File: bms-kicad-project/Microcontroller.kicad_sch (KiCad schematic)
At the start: 40 parts, among them J1 12402012E212A, J2 DEBUG, J3 Conn_02x18_Odd_Even, J4 Conn_02x18_Odd_Even, Q13 BSS308PE_H6327, SW1 KMR223G LFG, SW2 KMR223G LFG, U2 W25Q128JVSIQ TR, U3 NCP1117ST33T3G, U4 RP2040, X1 ABM8-272-T3

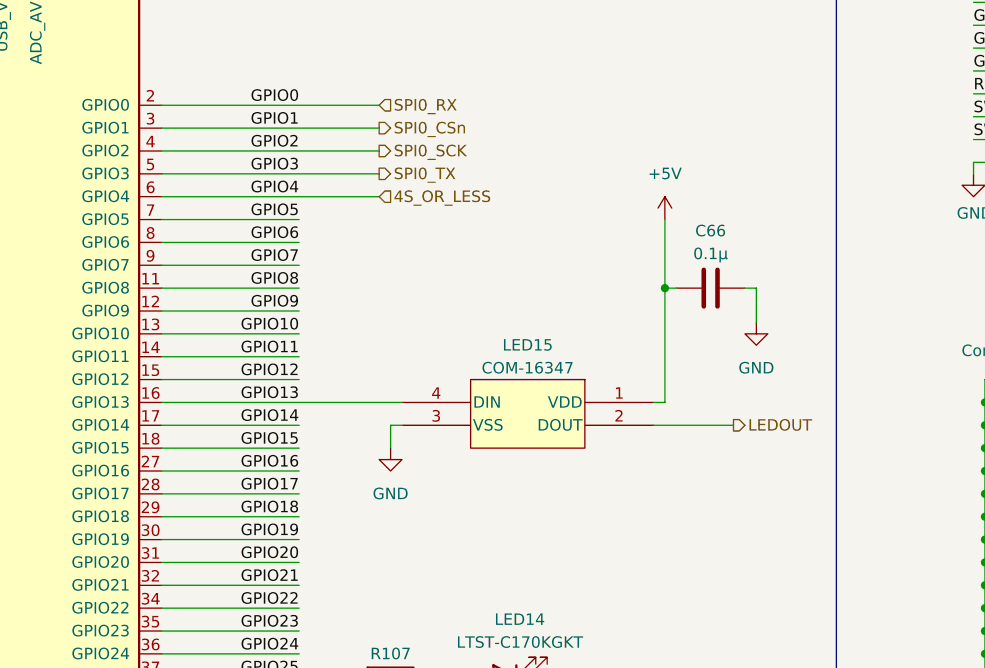
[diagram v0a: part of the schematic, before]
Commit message: Wired up most external connections
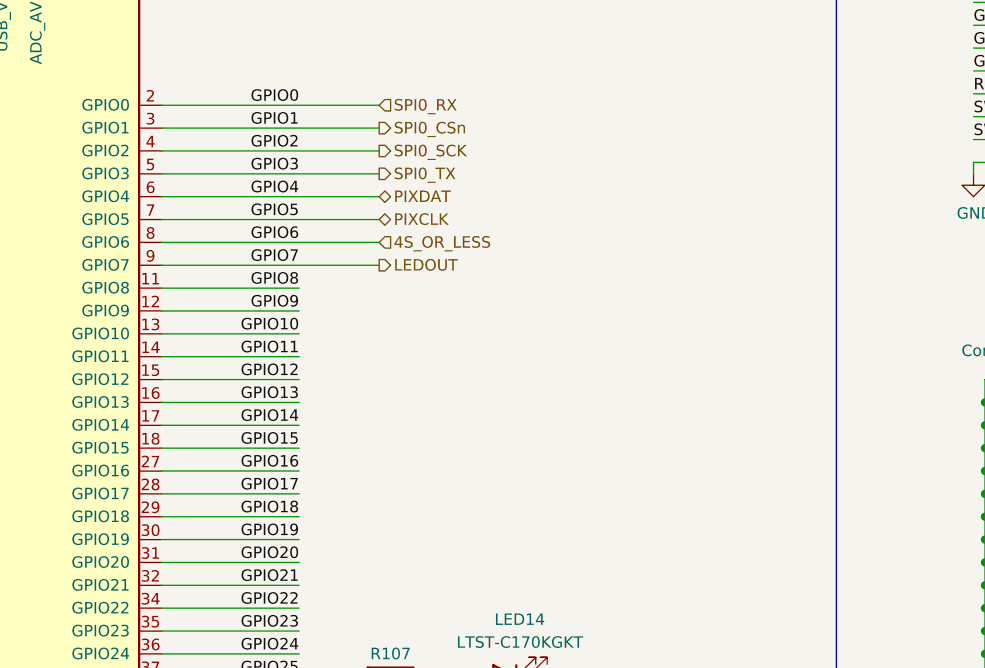
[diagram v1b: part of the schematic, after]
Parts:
- removed C66: 0.1µ, FixedWing:G-21_MUR, symbol FixedWing:GCM21BR72A104KA37L
- removed LED15: COM-16347, FixedWing:COM-16347_SPK, symbol FixedWing:COM-16347
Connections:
- net GPIO6 is gone; now on net 4S_OR_LESS: J3.16 (Pin_16), U4.8 (GPIO6)
- net GPIO7 is gone; now on net LEDOUT: J3.18 (Pin_18), U4.9 (GPIO7)
- net 4S_OR_LESS: no longer J3.12 (Pin_12), U4.6 (GPIO4)
- net GPIO5 renamed PIXCLK
- new net PIXDAT: J3.12 (Pin_12), U4.6 (GPIO4)
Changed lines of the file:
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@@
   (junction (at 26.67 146.05) (diameter 0) (color 0 0 0 0)
   )
-  (junction (at 344.17 123.19) (diameter 0) (color 0 0 0 0)
-  )
   (junction (at 405.13 81.28) (diameter 0) (color 0 0 0 0)
   )
@@
     (stroke (width 0) (type default))
   )
-  (wire (pts (xy 344.17 123.19) (xy 344.17 135.89))
-    (stroke (width 0) (type default))
-  )
   (wire (pts (xy 405.13 76.2) (xy 405.13 78.74))
     (stroke (width 0) (type default))
@@
     (stroke (width 0) (type default))
   )
-  (wire (pts (xy 342.9 138.43) (xy 351.79 138.43))
-    (stroke (width 0) (type default))
-  )
   (wire (pts (xy 288.29 166.37) (xy 309.88 166.37))
     (stroke (width 0) (type default))
   )
-  (wire (pts (xy 344.17 123.19) (xy 344.17 115.57))
-    (stroke (width 0) (type default))
-  )
   (wire (pts (xy 247.65 72.39) (xy 254 72.39))
     (stroke (width 0) (type default))
@@
     (stroke (width 0) (type default))
   )
+  (wire (pts (xy 288.29 120.65) (xy 312.42 120.65))
+    (stroke (width 0) (type default))
+  )
   (wire (pts (xy 55.88 128.27) (xy 55.88 121.92))
     (stroke (width 0) (type default))
@@
     (stroke (width 0) (type default))
   )
-  (wire (pts (xy 342.9 135.89) (xy 344.17 135.89))
-    (stroke (width 0) (type default))
-  )
   (wire (pts (xy 259.08 85.09) (xy 259.08 72.39))
     (stroke (width 0) (type default))
@@
     (stroke (width 0) (type default))
   )
+  (wire (pts (xy 288.29 135.89) (xy 303.53 135.89))
+    (stroke (width 0) (type default))
+  )
   (wire (pts (xy 147.32 137.16) (xy 147.32 165.1))
     (stroke (width 0) (type default))
@@
     (stroke (width 0) (type default))
   )
-  (wire (pts (xy 344.17 123.19) (xy 345.44 123.19))
-    (stroke (width 0) (type default))
-  )
   (wire (pts (xy 55.88 130.81) (xy 55.88 139.7))
     (stroke (width 0) (type default))
@@
     (stroke (width 0) (type default))
   )
-  (wire (pts (xy 313.69 138.43) (xy 313.69 140.97))
-    (stroke (width 0) (type default))
-  )
   (wire (pts (xy 379.73 163.83) (xy 379.73 166.37))
     (stroke (width 0) (type default))
@@
     (stroke (width 0) (type default))
   )
-  (wire (pts (xy 288.29 118.11) (xy 303.53 118.11))
+  (wire (pts (xy 288.29 118.11) (xy 312.42 118.11))
     (stroke (width 0) (type default))
   )
@@
     (stroke (width 0) (type default))
   )
-  (wire (pts (xy 288.29 120.65) (xy 303.53 120.65))
-    (stroke (width 0) (type default))
-  )
   (wire (pts (xy 227.33 68.58) (xy 227.33 67.31))
     (stroke (width 0) (type default))
@@
     (stroke (width 0) (type default))
   )
-  (wire (pts (xy 354.33 123.19) (xy 353.06 123.19))
-    (stroke (width 0) (type default))
-  )
   (wire (pts (xy 391.16 93.98) (xy 378.46 93.98))
     (stroke (width 0) (type default))
@@
     (stroke (width 0) (type default))
   )
-  (wire (pts (xy 288.29 135.89) (xy 314.96 135.89))
-    (stroke (width 0) (type default))
-  )
   (wire (pts (xy 339.09 54.61) (xy 327.66 54.61))
     (stroke (width 0) (type default))
@@
     (stroke (width 0) (type default))
   )
-  (wire (pts (xy 288.29 115.57) (xy 303.53 115.57))
+  (wire (pts (xy 288.29 115.57) (xy 312.42 115.57))
     (stroke (width 0) (type default))
   )
@@
     (stroke (width 0) (type default))
   )
-  (wire (pts (xy 314.96 138.43) (xy 313.69 138.43))
-    (stroke (width 0) (type default))
-  )
   (wire (pts (xy 36.83 160.02) (xy 142.24 160.02))
     (stroke (width 0) (type default))
@@
     (stroke (width 0) (type default))
   )
-  (wire (pts (xy 354.33 123.19) (xy 354.33 127))
-    (stroke (width 0) (type default))
-  )
   (wire (pts (xy 316.23 52.07) (xy 316.23 54.61))
     (stroke (width 0) (type default))
@@
     (effects (font (size 1.27 1.27)) (justify left))
   )
-  (hierarchical_label "SPI0_SCK" (shape output) (at 312.42 107.95 0) (fields_autoplaced)
+  (hierarchical_label "LEDOUT" (shape output) (at 312.42 120.65 0) (fields_autoplaced)
     (effects (font (size 1.27 1.27)) (justify left))
   )
-  (hierarchical_label "LEDOUT" (shape output) (at 351.79 138.43 0) (fields_autoplaced)
+  (hierarchical_label "SPI0_SCK" (shape output) (at 312.42 107.95 0) (fields_autoplaced)
     (effects (font (size 1.27 1.27)) (justify left))
   )
-  (hierarchical_label "4S_OR_LESS" (shape input) (at 312.42 113.03 0) (fields_autoplaced)
+  (hierarchical_label "4S_OR_LESS" (shape input) (at 312.42 118.11 0) (fields_autoplaced)
     (effects (font (size 1.27 1.27)) (justify left))
   )
@@
     (effects (font (size 1.27 1.27)) (justify left))
   )
+  (hierarchical_label "PIXDAT" (shape bidirectional) (at 312.42 113.03 0) (fields_autoplaced)
+    (effects (font (size 1.27 1.27)) (justify left))
+  )
+  (hierarchical_label "PIXCLK" (shape bidirectional) (at 312.42 115.57 0) (fields_autoplaced)
+    (effects (font (size 1.27 1.27)) (justify left))
+  )
   (hierarchical_label "SPI0_RX" (shape input) (at 312.42 102.87 0) (fields_autoplaced)
     (effects (font (size 1.27 1.27)) (justify left))
@@
     )
   )
-  (symbol (lib_id "power:+5V") (at 344.17 115.57 0) (unit 1)
-    (in_bom yes) (on_board yes) (dnp no) (fields_autoplaced)
-    (property "Reference" "#PWR062" (at 344.17 119.38 0)
-      (effects (font (size 1.27 1.27)) hide)
-    )
-    (property "Value" "+5V" (at 344.17 110.49 0)
-      (effects (font (size 1.27 1.27)))
-    )
-    (property "Footprint" "" (at 344.17 115.57 0)
-      (effects (font (size 1.27 1.27)) hide)
-    )
-    (property "Datasheet" "" (at 344.17 115.57 0)
-      (effects (font (size 1.27 1.27)) hide)
-    )
-    (pin "1")
-    (instances
-      (project "bms-board"
-        (path "/8a7831d1-a913-4f04-8780-225d2234b41d/449bb263-23d7-4f07-b4f7-6cd2e161d267"
-          (reference "#PWR062") (unit 1)
-        )
-      )
-    )
-  )
-  (symbol (lib_id "FixedWing:COM-16347") (at 342.9 135.89 0) (mirror y) (unit 1)
-    (in_bom yes) (on_board yes) (dnp no)
-    (property "Reference" "LED15" (at 328.93 129.54 0)
-      (effects (font (size 1.27 1.27)))
-    )
-    (property "Value" "COM-16347" (at 328.93 132.08 0)
-      (effects (font (size 1.27 1.27)))
-    )
-    (property "Footprint" "FixedWing:COM-16347_SPK" (at 342.9 123.19 0)
-      (effects (font (size 1.27 1.27) italic) hide)
-    )
-    (property "Datasheet" "https://cdn.sparkfun.com/datasheets/BreakoutBoards/WS2812B.pdf" (at 342.9 123.19 0)
-      (effects (font (size 1.27 1.27) italic) hide)
-    )
-    (property "Manufacturer" "SparkFun Electronics" (at 342.9 123.19 0)
-      (effects (font (size 1.27 1.27)) hide)
-    )
-    (property "Manufacturer Part Number" "COM-16347" (at 342.9 123.19 0)
-      (effects (font (size 1.27 1.27)) hide)
-    )
-    (pin "4")
-    (pin "3")
-    (pin "2")
-    (pin "1")
-    (instances
-      (project "bms-board"
-        (path "/8a7831d1-a913-4f04-8780-225d2234b41d/449bb263-23d7-4f07-b4f7-6cd2e161d267"
-          (reference "LED15") (unit 1)
-        )
-      )
-    )
-  )
   (symbol (lib_id "power:GND") (at 336.55 170.18 0) (unit 1)
     (in_bom yes) (on_board yes) (dnp no) (fields_autoplaced)
@@
     )
   )
-  (symbol (lib_id "power:GND") (at 313.69 140.97 0) (unit 1)
-    (in_bom yes) (on_board yes) (dnp no) (fields_autoplaced)
-    (property "Reference" "#PWR063" (at 313.69 147.32 0)
-      (effects (font (size 1.27 1.27)) hide)
-    )
-    (property "Value" "GND" (at 313.69 146.05 0)
-      (effects (font (size 1.27 1.27)))
-    )
-    (property "Footprint" "" (at 313.69 140.97 0)
-      (effects (font (size 1.27 1.27)) hide)
-    )
-    (property "Datasheet" "" (at 313.69 140.97 0)
-      (effects (font (size 1.27 1.27)) hide)
-    )
-    (pin "1")
-    (instances
-      (project "bms-board"
-        (path "/8a7831d1-a913-4f04-8780-225d2234b41d/449bb263-23d7-4f07-b4f7-6cd2e161d267"
-          (reference "#PWR063") (unit 1)
-        )
-      )
-    )
-  )
   (symbol (lib_id "FixedWing:KMR223G_LFG") (at 57.15 128.27 0) (unit 1)
     (in_bom yes) (on_board yes) (dnp no)
@@
     )
   )
-  (symbol (lib_id "power:GND") (at 354.33 127 0) (unit 1)
-    (in_bom yes) (on_board yes) (dnp no) (fields_autoplaced)
-    (property "Reference" "#PWR064" (at 354.33 133.35 0)
-      (effects (font (size 1.27 1.27)) hide)
-    )
-    (property "Value" "GND" (at 354.33 132.08 0)
-      (effects (font (size 1.27 1.27)))
-    )
-    (property "Footprint" "" (at 354.33 127 0)
-      (effects (font (size 1.27 1.27)) hide)
-    )
-    (property "Datasheet" "" (at 354.33 127 0)
-      (effects (font (size 1.27 1.27)) hide)
-    )
-    (pin "1")
-    (instances
-      (project "bms-board"
-        (path "/8a7831d1-a913-4f04-8780-225d2234b41d/449bb263-23d7-4f07-b4f7-6cd2e161d267"
-          (reference "#PWR064") (unit 1)
-        )
-      )
-    )
-  )
   (symbol (lib_id "FixedWing:RK73H2ATTD5601F") (at 59.69 86.36 90) (unit 1)
     (in_bom yes) (on_board yes) (dnp no)
@@
         )
       )
-    )
-  )
-  (symbol (lib_id "FixedWing:GCM21BR72A104KA37L") (at 353.06 123.19 180) (unit 1)
-    (in_bom yes) (on_board yes) (dnp no)
-    (property "Reference" "C66" (at 349.25 116.84 0)
-      (effects (font (size 1.27 1.27)))
-    )
-    (property "Value" "0.1µ" (at 349.25 119.38 0)
-      (effects (font (size 1.27 1.27)))
-    )
-    (property "Footprint" "FixedWing:G-21_MUR" (at 353.06 137.16 0)
-      (effects (font (size 1.27 1.27) italic) hide)
-    )
-    (property "Datasheet" "https://search.murata.co.jp/Ceramy/image/img/A01X/G101/ENG/GCJ21BR71A106KE01-01A.pdf" (at 353.06 134.62 0)
-      (effects (font (size 1.27 1.27) italic) hide)
-    )
-    (property "Manufacturer" "Murata Electronics" (at 353.06 132.08 0)
-      (effects (font (size 1.27 1.27)) hide)
-    )
-    (property "Manufacturer Part Number" "GCM21BR72A104KA37L" (at 353.06 129.54 0)
-      (effects (font (size 1.27 1.27)) hide)
-    )
-    (pin "1")
-    (pin "2")
-    (instances
-      (project "bms-board"
-        (path "/8a7831d1-a913-4f04-8780-225d2234b41d/449bb263-23d7-4f07-b4f7-6cd2e161d267"
-          (reference "C66") (unit 1)
-        )
-      )

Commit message: feat: Just shifting a few things around
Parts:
- renumbered C15 to C22, C16 to C23, C17 to C24, C18 to C25, C19 to C26, C20 to C27, C21 to C28, C22 to C29, C23 to C30, C24 to C31, C25 to C32, C26 to C33, C27 to C34, C28 to C35, C29 to C36, C30 to C37, C31 to C38, J1 to J2, J2 to J3, J3 to J4, J4 to J5, LED14 to LED13, Q13 to Q14, R77 to R84, R78 to R85, R79 to R86, R80 to R87, R81 to R88, R82 to R89, R83 to R90, R107 to R91, U2 to U4, U3 to U5, U4 to U6

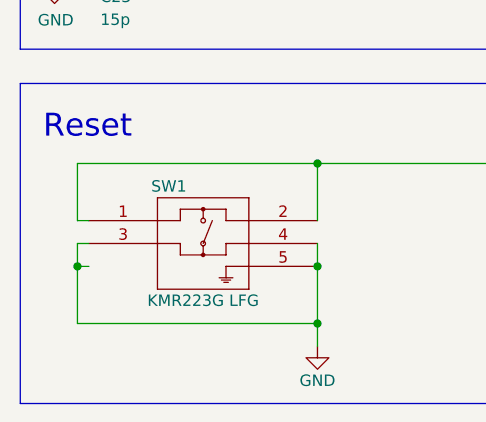
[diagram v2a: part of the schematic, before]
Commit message: feat: added sims directory, new cell balancing components
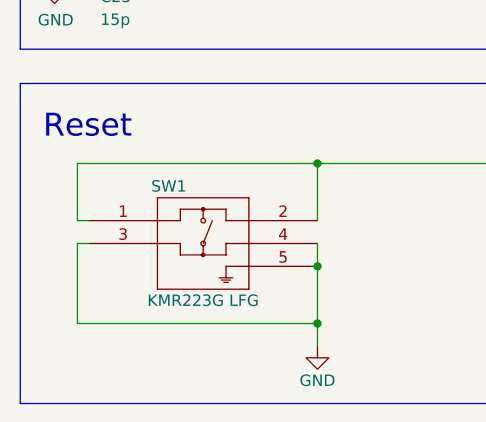
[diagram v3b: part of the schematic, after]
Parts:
- C24, C28, C29, C31, C33, C34, C35, C36, C37, C38: Manufacturer Part Number (none) -> GCJ188R72A104KA01D
- Q14: Manufacturer (none) -> Infineon; Manufacturer Part Number (none) -> BSS308PE H6327
- R86, R87: Manufacturer Part Number (none) -> RC0805FR-071KL
- R89, R90: Manufacturer Part Number (none) -> RC0805FR-0727RL
- R91: Manufacturer (none) -> Vishay; Manufacturer Part Number (none) -> CRCW0805475RFKEA
- SW1, SW2: Manufacturer Part Number (none) -> KMR223GLFG
- U4: Manufacturer Part Number (none) -> W25Q128JVSIQ TR
- U6: Manufacturer Part Number (none) -> SC0914(13)
- X1: Manufacturer Part Number (none) -> ABM8-272-T3
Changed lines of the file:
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@@
   (junction (at 274.32 72.39) (diameter 0) (color 0 0 0 0)
   )
-  (junction (at 21.59 248.92) (diameter 0) (color 0 0 0 0)
-  )
   (junction (at 34.29 195.58) (diameter 0) (color 0 0 0 0)
   )
@@
     (stroke (width 0) (type default))
   )
-  (wire (pts (xy 21.59 248.92) (xy 22.86 248.92))
-    (stroke (width 0) (type default))
-  )
   (wire (pts (xy 82.55 130.81) (xy 83.82 130.81))
     (stroke (width 0) (type default))
@@
     (stroke (width 0) (type default))
   )
-  (wire (pts (xy 21.59 246.38) (xy 21.59 248.92))
-    (stroke (width 0) (type default))
-  )
   (wire (pts (xy 288.29 151.13) (xy 303.53 151.13))
     (stroke (width 0) (type default))
@@
     (stroke (width 0) (type default))
   )
-  (wire (pts (xy 21.59 248.92) (xy 21.59 255.27))
+  (wire (pts (xy 21.59 246.38) (xy 21.59 255.27))
     (stroke (width 0) (type default))
   )
@@
       (effects (font (size 1.27 1.27)) hide)
     )
+    (property "Manufacturer Part Number" "SC0914(13)" (at 256.54 135.89 0)
+      (effects (font (size 1.27 1.27)) hide)
+    )
     (pin "1")
     (pin "10")
@@
       (effects (font (size 1.27 1.27)) hide)
     )
+    (property "Manufacturer Part Number" "W25Q128JVSIQ TR" (at 26.67 133.35 0)
+      (effects (font (size 1.27 1.27)) hide)
+    )
     (pin "1")
     (pin "2")
@@
       (effects (font (size 1.27 1.27)) hide)
     )
+    (property "Manufacturer Part Number" "RC0805FR-071KL" (at 116.84 110.49 0)
+      (effects (font (size 1.27 1.27)) hide)
+    )
     (pin "1")
     (pin "2")
@@
       (effects (font (size 1.27 1.27)) hide)
     )
+    (property "Manufacturer Part Number" "GCJ188R72A104KA01D" (at 27.94 148.59 0)
+      (effects (font (size 1.27 1.27)) hide)
+    )
     (pin "1")
     (pin "2")
@@
       (effects (font (size 1.27 1.27)) hide)
     )
+    (property "Manufacturer Part Number" "RC0805FR-0727RL" (at 215.9 81.28 0)
+      (effects (font (size 1.27 1.27)) hide)
+    )
     (pin "1")
     (pin "2")
@@
       (effects (font (size 1.27 1.27)) hide)
     )
+    (property "Manufacturer Part Number" "RC0805FR-0727RL" (at 215.9 88.9 0)
+      (effects (font (size 1.27 1.27)) hide)
+    )
     (pin "1")
     (pin "2")
@@
       (effects (font (size 1.27 1.27)) hide)
     )
+    (property "Manufacturer Part Number" "GCJ188R72A104KA01D" (at 293.37 41.91 0)
+      (effects (font (size 1.27 1.27)) hide)
+    )
     (pin "1")
     (pin "2")
@@
       (effects (font (size 1.27 1.27)) hide)
     )
+    (property "Manufacturer Part Number" "GCJ188R72A104KA01D" (at 304.8 41.91 0)
+      (effects (font (size 1.27 1.27)) hide)
+    )
     (pin "1")
     (pin "2")
@@
       (effects (font (size 1.27 1.27)) hide)
     )
+    (property "Manufacturer Part Number" "GCJ188R72A104KA01D" (at 293.37 54.61 0)
+      (effects (font (size 1.27 1.27)) hide)
+    )
     (pin "1")
     (pin "2")
@@
       (effects (font (size 1.27 1.27)) hide)
     )
+    (property "Manufacturer Part Number" "GCJ188R72A104KA01D" (at 327.66 41.91 0)
+      (effects (font (size 1.27 1.27)) hide)
+    )
     (pin "1")
     (pin "2")
@@
       (effects (font (size 1.27 1.27)) hide)
     )
+    (property "Manufacturer Part Number" "GCJ188R72A104KA01D" (at 339.09 41.91 0)
+      (effects (font (size 1.27 1.27)) hide)
+    )
     (pin "1")
     (pin "2")
@@
       (effects (font (size 1.27 1.27)) hide)
     )
+    (property "Manufacturer Part Number" "GCJ188R72A104KA01D" (at 350.52 41.91 0)
+      (effects (font (size 1.27 1.27)) hide)
+    )
     (pin "1")
     (pin "2")
@@
       (effects (font (size 1.27 1.27)) hide)
     )
+    (property "Manufacturer Part Number" "GCJ188R72A104KA01D" (at 361.95 41.91 0)
+      (effects (font (size 1.27 1.27)) hide)
+    )
     (pin "1")
     (pin "2")
@@
       (effects (font (size 1.27 1.27)) hide)
     )
+    (property "Manufacturer Part Number" "GCJ188R72A104KA01D" (at 201.93 54.61 0)
+      (effects (font (size 1.27 1.27)) hide)
+    )
     (pin "1")
     (pin "2")
@@
       (effects (font (size 1.27 1.27)) hide)
     )
+    (property "Manufacturer Part Number" "GCJ188R72A104KA01D" (at 213.36 54.61 0)
+      (effects (font (size 1.27 1.27)) hide)
+    )
     (pin "1")
     (pin "2")
@@
       (effects (font (size 1.27 1.27)) hide)
     )
+    (property "Manufacturer Part Number" "ABM8-272-T3" (at 35.56 203.2 0)
+      (effects (font (size 1.27 1.27)) hide)
+    )
     (pin "1")
     (pin "2")
@@
       (effects (font (size 1.27 1.27)) hide)
     )
+    (property "Manufacturer Part Number" "KMR223GLFG" (at 57.15 128.27 0)
+      (effects (font (size 1.27 1.27)) hide)
+    )
     (pin "1")
     (pin "5")
@@
       (effects (font (size 1.27 1.27)) hide)
     )
+    (property "Manufacturer Part Number" "KMR223GLFG" (at 22.86 243.84 0)
+      (effects (font (size 1.27 1.27)) hide)
+    )
     (pin "3")
     (pin "4")
@@
       (effects (font (size 1.27 1.27)) hide)
     )
+    (property "Manufacturer Part Number" "RC0805FR-071KL" (at 74.93 203.2 0)
+      (effects (font (size 1.27 1.27)) hide)
+    )
     (pin "1")
     (pin "2")
@@
       (effects (font (size 1.27 1.27)) (justify left top) hide)
     )
+    (property "Manufacturer" "Vishay" (at 323.85 862.56 0)
+      (effects (font (size 1.27 1.27)) (justify left top) hide)
+    )
+    (property "Manufacturer Part Number" "CRCW0805475RFKEA" (at 323.85 962.56 0)
+      (effects (font (size 1.27 1.27)) (justify left top) hide)
+    )
     (pin "1")
     (pin "2")
@@
       (effects (font (size 1.27 1.27)) (justify left top) hide)
     )
+    (property "Manufacturer" "Infineon" (at 87.63 735.56 0)
+      (effects (font (size 1.27 1.27)) (justify left top) hide)
+    )
+    (property "Manufacturer Part Number" "BSS308PE H6327" (at 87.63 835.56 0)
+      (effects (font (size 1.27 1.27)) (justify left top) hide)
+    )
